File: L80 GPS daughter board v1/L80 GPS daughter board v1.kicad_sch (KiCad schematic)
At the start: 19 parts, among them J1 Conn_01x04_Pin, J2 THD2528-11SD-GF, J3 Conn_01x02_Pin, J4 Conn_01x07_Socket, SW1 SW_Push, U1 AP2112K-3.3, U2 L80-R, U3 MCP73831-2-OT, U4 AP2112K-3.3

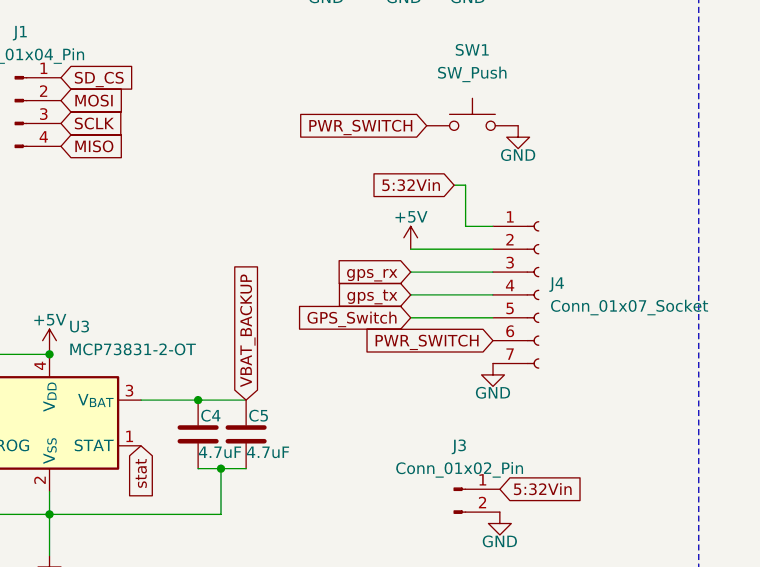
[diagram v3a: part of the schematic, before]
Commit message: modefied gps board pins
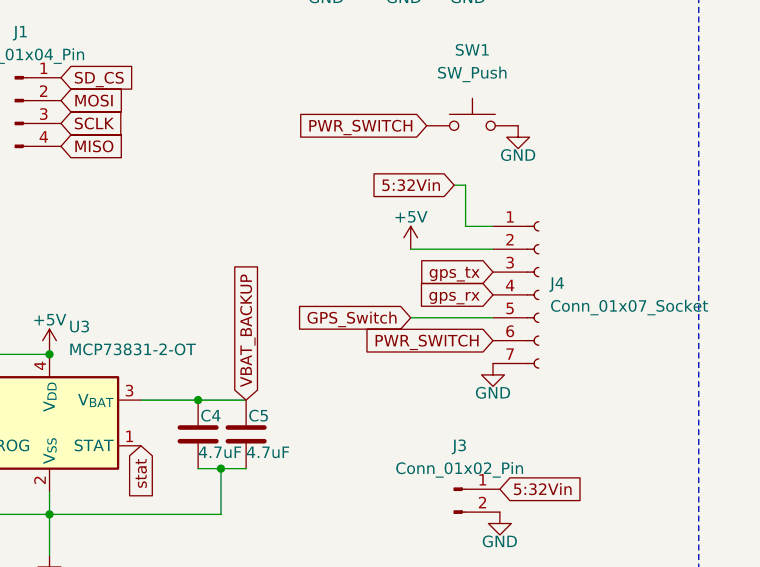
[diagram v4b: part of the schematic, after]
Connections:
- net gps_rx: now also J4.4 (Pin_4); no longer J4.3 (Pin_3)
- net gps_tx: now also J4.3 (Pin_3); no longer J4.4 (Pin_4)
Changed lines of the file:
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@@
-	(wire
-		(pts
-			(xy 189.23 104.14) (xy 180.086 104.14)
-		)
-		(stroke
-			(width 0)
-			(type default)
-		)
-	)
 	(wire
 		(pts
@@
 	(wire
 		(pts
-			(xy 189.23 101.6) (xy 180.086 101.6)
-		)
-		(stroke
-			(width 0)
-			(type default)
-		)
-	)
-	(wire
-		(pts
 			(xy 179.324 57.658) (xy 178.308 57.658)
 		)
@@
 	(global_label "gps_rx"
 		(shape input)
-		(at 180.086 101.6 180)
-		(fields_autoplaced yes)
-		(effects
-			(font
-				(size 1.27 1.27)
-			)
-			(justify right)
-		)
-		(property "Intersheetrefs" "${INTERSHEET_REFS}"
-			(at 170.9928 101.6 0)
+		(at 189.23 104.14 180)
+		(fields_autoplaced yes)
+		(effects
+			(font
+				(size 1.27 1.27)
+			)
+			(justify right)
+		)
+		(property "Intersheetrefs" "${INTERSHEET_REFS}"
+			(at 180.1368 104.14 0)
 			(effects
 				(font
@@
 	(global_label "gps_tx"
 		(shape input)
-		(at 180.086 104.14 180)
-		(fields_autoplaced yes)
-		(effects
-			(font
-				(size 1.27 1.27)
-			)
-			(justify right)
-		)
-		(property "Intersheetrefs" "${INTERSHEET_REFS}"
-			(at 171.0533 104.14 0)
-			(effects
-				(font
+		(at 189.23 101.6 180)
+		(fields_autoplaced yes)
+		(effects
+			(font
+				(size 1.27 1.27)
+			)
+			(justify right)
+		)
+		(property "Intersheetrefs" "${INTERSHEET_REFS}"
+			(at 180.1973 101.6 0)
+			(effects
+				(font
